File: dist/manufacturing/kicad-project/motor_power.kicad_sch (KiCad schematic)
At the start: 25 parts, among them Q4 CSD19534Q5A, Q5 Q5, U6 TPS26631RGER

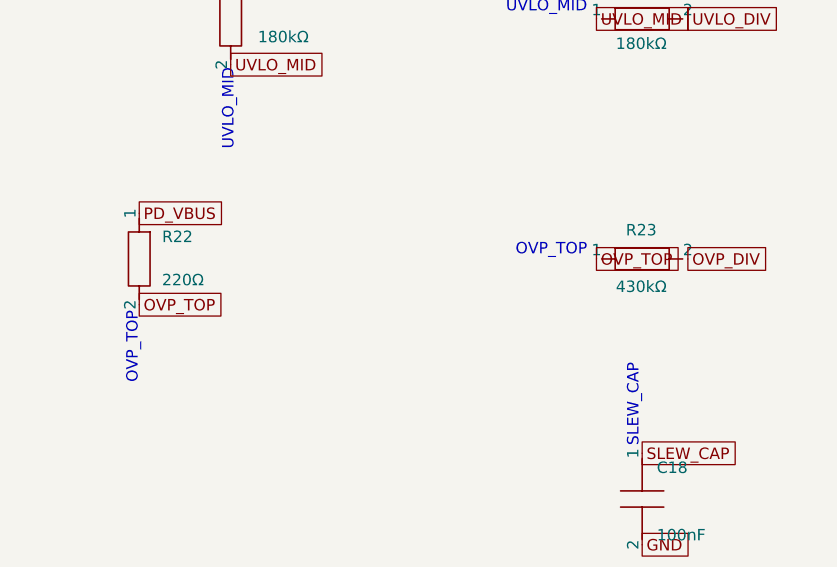
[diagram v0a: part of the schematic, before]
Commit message: Correct driver supply and brake protection power limits
Add the regulated 12 V TMC5160 gate supply and precision brake/OVP thresholds. Refresh top-side routing and manufacturing outputs with zero native DRC/ERC and complete connectivity. Verify native bypass paths and document calculations, sourcing, order holds, and unperformed powered tests.
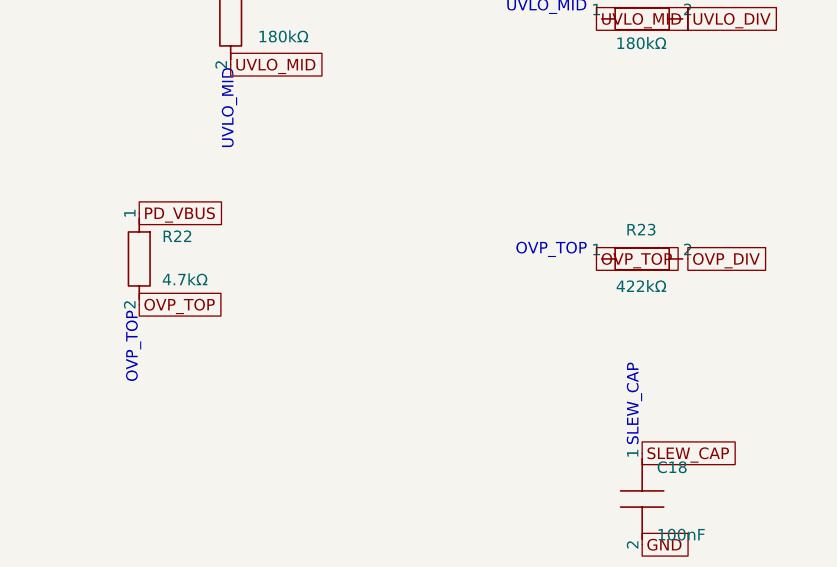
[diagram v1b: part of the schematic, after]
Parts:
- R22: value 220Ω -> 4.7kΩ
- R23: value 430kΩ -> 422kΩ
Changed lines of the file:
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@@
     (instances
       (project ""
-        (path "/953e0ace-4c89-4879-a4e2-9aa73ffc3208/3857d395-d674-4195-b5e4-44b57166172a"
+        (path "/c04facae-e812-4ae4-9853-e4e120a44c97/a986f742-2c88-45ac-8531-5c55a8ba8818"
           (reference "Q4")
           (unit 1)
@@
     (instances
       (project ""
-        (path "/953e0ace-4c89-4879-a4e2-9aa73ffc3208/3857d395-d674-4195-b5e4-44b57166172a"
+        (path "/c04facae-e812-4ae4-9853-e4e120a44c97/a986f742-2c88-45ac-8531-5c55a8ba8818"
           (reference "Q5")
           (unit 1)
@@
     (instances
       (project ""
-        (path "/953e0ace-4c89-4879-a4e2-9aa73ffc3208/3857d395-d674-4195-b5e4-44b57166172a"
+        (path "/c04facae-e812-4ae4-9853-e4e120a44c97/a986f742-2c88-45ac-8531-5c55a8ba8818"
           (reference "U6")
           (unit 1)
@@
     (instances
       (project ""
-        (path "/953e0ace-4c89-4879-a4e2-9aa73ffc3208/3857d395-d674-4195-b5e4-44b57166172a"
+        (path "/c04facae-e812-4ae4-9853-e4e120a44c97/a986f742-2c88-45ac-8531-5c55a8ba8818"
           (reference "R19")
           (unit 1)
@@
     (instances
       (project ""
-        (path "/953e0ace-4c89-4879-a4e2-9aa73ffc3208/3857d395-d674-4195-b5e4-44b57166172a"
+        (path "/c04facae-e812-4ae4-9853-e4e120a44c97/a986f742-2c88-45ac-8531-5c55a8ba8818"
           (reference "R20")
           (unit 1)
@@
     (instances
       (project ""
-        (path "/953e0ace-4c89-4879-a4e2-9aa73ffc3208/3857d395-d674-4195-b5e4-44b57166172a"
+        (path "/c04facae-e812-4ae4-9853-e4e120a44c97/a986f742-2c88-45ac-8531-5c55a8ba8818"
           (reference "R21")
           (unit 1)
@@
       )
     )
-    (property "Value" "220Ω"
+    (property "Value" "4.7kΩ"
       (id 1)
       (at 375.9075 157.275 0)
@@
     (instances
       (project ""
-        (path "/953e0ace-4c89-4879-a4e2-9aa73ffc3208/3857d395-d674-4195-b5e4-44b57166172a"
+        (path "/c04facae-e812-4ae4-9853-e4e120a44c97/a986f742-2c88-45ac-8531-5c55a8ba8818"
           (reference "R22")
           (unit 1)
@@
       )
     )
-    (property "Value" "430kΩ"
+    (property "Value" "422kΩ"
       (id 1)
       (at 429.1575 157.275 0)
@@
     (instances
       (project ""
-        (path "/953e0ace-4c89-4879-a4e2-9aa73ffc3208/3857d395-d674-4195-b5e4-44b57166172a"
+        (path "/c04facae-e812-4ae4-9853-e4e120a44c97/a986f742-2c88-45ac-8531-5c55a8ba8818"
           (reference "R23")
           (unit 1)
@@
     (instances
       (project ""
-        (path "/953e0ace-4c89-4879-a4e2-9aa73ffc3208/3857d395-d674-4195-b5e4-44b57166172a"
+        (path "/c04facae-e812-4ae4-9853-e4e120a44c97/a986f742-2c88-45ac-8531-5c55a8ba8818"
           (reference "R24")
           (unit 1)
@@
     (instances
       (project ""
-        (path "/953e0ace-4c89-4879-a4e2-9aa73ffc3208/3857d395-d674-4195-b5e4-44b57166172a"
+        (path "/c04facae-e812-4ae4-9853-e4e120a44c97/a986f742-2c88-45ac-8531-5c55a8ba8818"
           (reference "R25")
           (unit 1)
@@
     (instances
       (project ""
-        (path "/953e0ace-4c89-4879-a4e2-9aa73ffc3208/3857d395-d674-4195-b5e4-44b57166172a"
+        (path "/c04facae-e812-4ae4-9853-e4e120a44c97/a986f742-2c88-45ac-8531-5c55a8ba8818"
           (reference "C18")
           (unit 1)
@@
     (instances
       (project ""
-        (path "/953e0ace-4c89-4879-a4e2-9aa73ffc3208/3857d395-d674-4195-b5e4-44b57166172a"
+        (path "/c04facae-e812-4ae4-9853-e4e120a44c97/a986f742-2c88-45ac-8531-5c55a8ba8818"
           (reference "R26")
           (unit 1)
@@
     (instances
       (project ""
-        (path "/953e0ace-4c89-4879-a4e2-9aa73ffc3208/3857d395-d674-4195-b5e4-44b57166172a"
+        (path "/c04facae-e812-4ae4-9853-e4e120a44c97/a986f742-2c88-45ac-8531-5c55a8ba8818"
           (reference "C19")
           (unit 1)
@@
     (instances
       (project ""
-        (path "/953e0ace-4c89-4879-a4e2-9aa73ffc3208/3857d395-d674-4195-b5e4-44b57166172a"
+        (path "/c04facae-e812-4ae4-9853-e4e120a44c97/a986f742-2c88-45ac-8531-5c55a8ba8818"
           (reference "R27")
           (unit 1)
@@
     (instances
       (project ""
-        (path "/953e0ace-4c89-4879-a4e2-9aa73ffc3208/3857d395-d674-4195-b5e4-44b57166172a"
+        (path "/c04facae-e812-4ae4-9853-e4e120a44c97/a986f742-2c88-45ac-8531-5c55a8ba8818"
           (reference "R28")
           (unit 1)
@@
     (instances
       (project ""
-        (path "/953e0ace-4c89-4879-a4e2-9aa73ffc3208/3857d395-d674-4195-b5e4-44b57166172a"
+        (path "/c04facae-e812-4ae4-9853-e4e120a44c97/a986f742-2c88-45ac-8531-5c55a8ba8818"
           (reference "R29")
           (unit 1)
@@
     (instances
       (project ""
-        (path "/953e0ace-4c89-4879-a4e2-9aa73ffc3208/3857d395-d674-4195-b5e4-44b57166172a"
+        (path "/c04facae-e812-4ae4-9853-e4e120a44c97/a986f742-2c88-45ac-8531-5c55a8ba8818"
           (reference "R30")
           (unit 1)
@@
     (instances
       (project ""
-        (path "/953e0ace-4c89-4879-a4e2-9aa73ffc3208/3857d395-d674-4195-b5e4-44b57166172a"
+        (path "/c04facae-e812-4ae4-9853-e4e120a44c97/a986f742-2c88-45ac-8531-5c55a8ba8818"
           (reference "C20")
           (unit 1)
@@
     (instances
       (project ""
-        (path "/953e0ace-4c89-4879-a4e2-9aa73ffc3208/3857d395-d674-4195-b5e4-44b57166172a"
+        (path "/c04facae-e812-4ae4-9853-e4e120a44c97/a986f742-2c88-45ac-8531-5c55a8ba8818"
           (reference "C21")
           (unit 1)
@@
     (instances
       (project ""
-        (path "/953e0ace-4c89-4879-a4e2-9aa73ffc3208/3857d395-d674-4195-b5e4-44b57166172a"
+        (path "/c04facae-e812-4ae4-9853-e4e120a44c97/a986f742-2c88-45ac-8531-5c55a8ba8818"
           (reference "C22")
           (unit 1)
@@
     (instances
       (project ""
-        (path "/953e0ace-4c89-4879-a4e2-9aa73ffc3208/3857d395-d674-4195-b5e4-44b57166172a"
+        (path "/c04facae-e812-4ae4-9853-e4e120a44c97/a986f742-2c88-45ac-8531-5c55a8ba8818"
           (reference "C23")
           (unit 1)
@@
     (instances
       (project ""
-        (path "/953e0ace-4c89-4879-a4e2-9aa73ffc3208/3857d395-d674-4195-b5e4-44b57166172a"
+        (path "/c04facae-e812-4ae4-9853-e4e120a44c97/a986f742-2c88-45ac-8531-5c55a8ba8818"
           (reference "R31")
           (unit 1)
@@
     (instances
       (project ""
-        (path "/953e0ace-4c89-4879-a4e2-9aa73ffc3208/3857d395-d674-4195-b5e4-44b57166172a"
+        (path "/c04facae-e812-4ae4-9853-e4e120a44c97/a986f742-2c88-45ac-8531-5c55a8ba8818"
           (reference "R32")
           (unit 1)
@@
     (instances
       (project ""
-        (path "/953e0ace-4c89-4879-a4e2-9aa73ffc3208/3857d395-d674-4195-b5e4-44b57166172a"
+        (path "/c04facae-e812-4ae4-9853-e4e120a44c97/a986f742-2c88-45ac-8531-5c55a8ba8818"
           (reference "R33")
           (unit 1)
@@
     (instances
       (project ""
-        (path "/953e0ace-4c89-4879-a4e2-9aa73ffc3208/3857d395-d674-4195-b5e4-44b57166172a"
+        (path "/c04facae-e812-4ae4-9853-e4e120a44c97/a986f742-2c88-45ac-8531-5c55a8ba8818"
           (reference "C24")
           (unit 1)

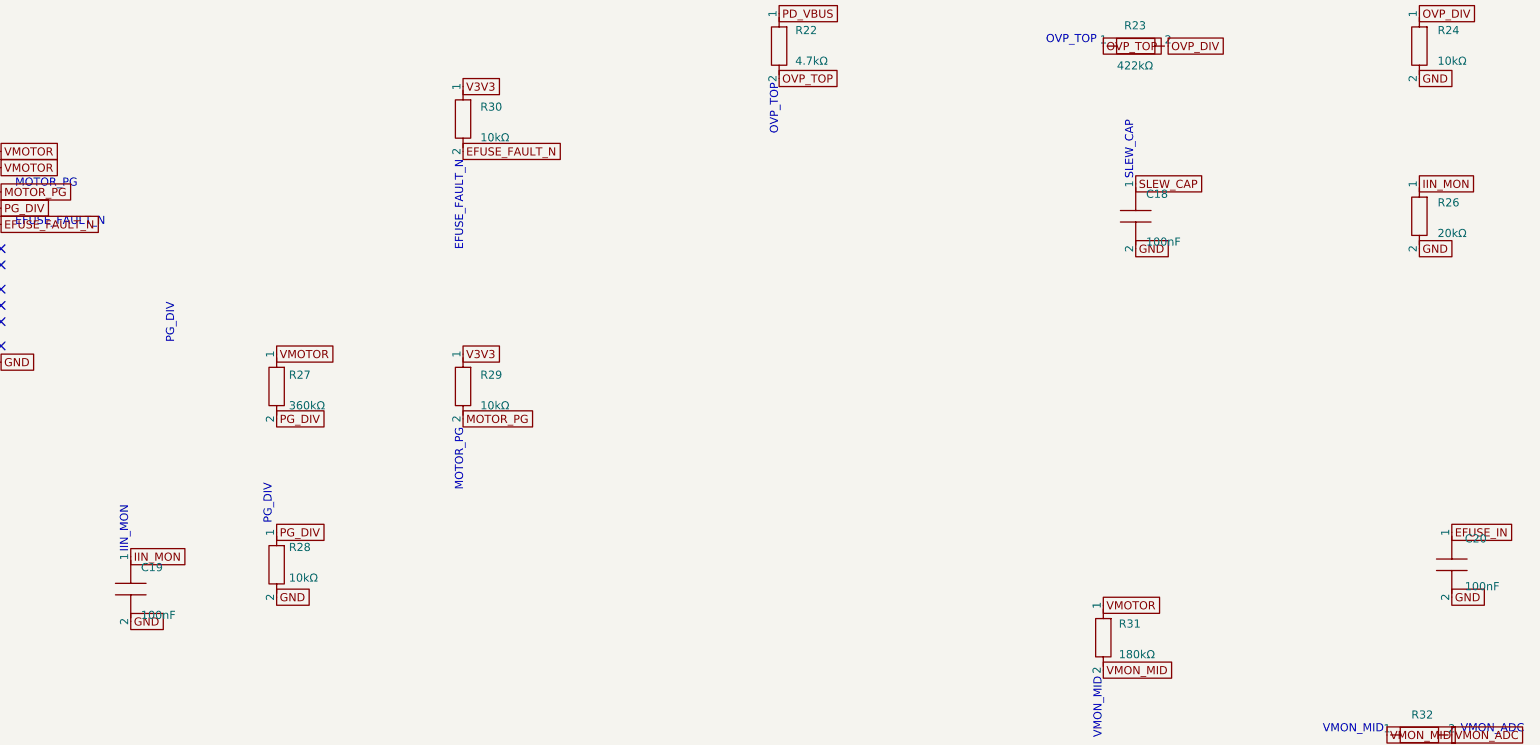
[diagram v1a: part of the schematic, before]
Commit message: Remove IMON bypass and prepare pre-shipment test handoff
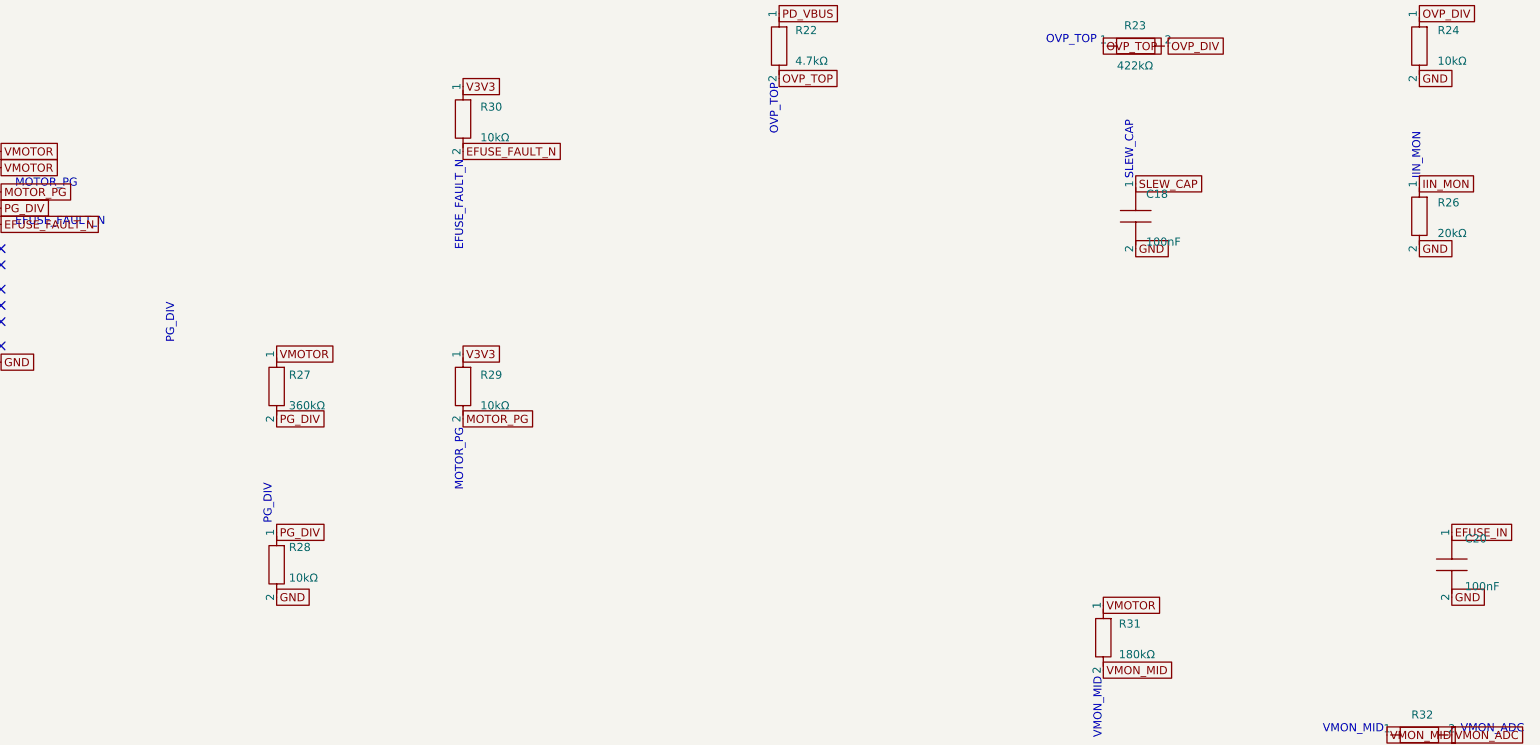
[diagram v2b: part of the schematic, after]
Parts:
- removed C19: 100nF, capacitor_cap0603, symbol Device:capacitor_down

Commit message: Fix source warnings and organize schematic on A4 sheets
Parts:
- removed Q4: CSD19534Q5A, CSD19534Q5A, symbol Device:U_CSD19534Q5A
- added Q4: CSD19534Q5A, CSD19534Q5A, symbol Custom:CSD19534Q5A
- Q5: value Q5 -> BSS123LT1G
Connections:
- net BLOCK_GATE: now also Q4.4 (G)
- net EFUSE_IN: now also Q4.5 (D1), Q4.6 (D2), Q4.7 (D3), Q4.8 (D4), Q4.9 (D5)
- net PD_VBUS: now also Q4.1 (S1), Q4.2 (S2), Q4.3 (S3)
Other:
- note added: "06 / Protected 48 V Motor Bus"
- note added: "Nominal current limit 4.48 A. C22/C23 are motor bulk; R31-R33/C24 monitor voltage."
- note added: "Q4/Q5 provide reverse blocking; U6 is the eFuse and input-current monitor."
- note removed: "03 / Protected 48 V Motor Bus"
- note removed: "Nominal eFuse limit 4.48 A. No reverse energy into the USB source."
- note removed: "Q4: reverse-blocking power MOSFET. Q5: fast gate clamp. U6: TPS26631 48 V eFuse, current monitor and fault output."
